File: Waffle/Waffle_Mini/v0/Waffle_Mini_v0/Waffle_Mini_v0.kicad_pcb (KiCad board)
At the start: 2 copper layers, 16 parts, among them J1 cJTAG, U1 F2800154QRHBRQ1, U2 AP7375-33SA-7

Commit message: Layout kinda done v0 waffle mini
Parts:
- removed C4, C7: 100n, Capacitor_SMD:C_0603_1608Metric
- removed C8: 10u, Capacitor_SMD:C_0805_2012Metric
- added J10: Conn_01x01_Socket, ICDB_Waffle:ICDB_Castellated_Pad, F.Cu at (139.7, 104.1)
- added J11: Conn_01x01_Socket, ICDB_Waffle:ICDB_Castellated_Pad, F.Cu at (142.2, 104.1)
- added J12: Conn_01x01_Socket, ICDB_Waffle:ICDB_Castellated_Pad, F.Cu at (144.8, 104.1)
- added J13: Conn_01x01_Socket, ICDB_Waffle:ICDB_Castellated_Pad, F.Cu at (147.3, 104.1)
- added J14: Conn_01x01_Socket, ICDB_Waffle:ICDB_Castellated_Pad, F.Cu at (149.9, 104.1)
- added J15: Conn_01x01_Socket, ICDB_Waffle:ICDB_Castellated_Pad, F.Cu at (152.4, 104.1)
- added J16: Conn_01x01_Socket, ICDB_Waffle:ICDB_Castellated_Pad, F.Cu at (154.9, 104.1)
- added J17: Conn_01x01_Socket, ICDB_Waffle:ICDB_Castellated_Pad, F.Cu at (157.5, 104.1)
- added J18: Conn_01x01_Socket, ICDB_Waffle:ICDB_Castellated_Pad, F.Cu at (160.0, 104.1)
- added J19: Conn_01x01_Socket, ICDB_Waffle:ICDB_Castellated_Pad, F.Cu at (162.6, 104.1)
- added J2: Conn_01x01_Socket, ICDB_Waffle:ICDB_Castellated_Pad, F.Cu at (157.5, 86.4)
- added J20: Conn_01x01_Socket, ICDB_Waffle:ICDB_Castellated_Pad, F.Cu at (165.1, 104.1)
- added J21: Conn_01x01_Socket, ICDB_Waffle:ICDB_Castellated_Pad, F.Cu at (165.1, 86.4)
- added J22: Conn_01x01_Socket, ICDB_Waffle:ICDB_Castellated_Pad, F.Cu at (162.6, 86.4)
- added J23: Conn_01x01_Socket, ICDB_Waffle:ICDB_Castellated_Pad, F.Cu at (160.0, 86.4)
- added J24: Conn_01x01_Socket, ICDB_Waffle:ICDB_Castellated_Pad, F.Cu at (134.6, 86.4)
- added J25: Conn_01x01_Socket, ICDB_Waffle:ICDB_Castellated_Pad, F.Cu at (134.6, 104.1)
- added J26: Conn_01x01_Socket, ICDB_Waffle:ICDB_Castellated_Pad, F.Cu at (137.2, 86.4)
- added J27: Conn_01x01_Socket, ICDB_Waffle:ICDB_Castellated_Pad, F.Cu at (137.2, 104.1)
- added J28: Conn_01x01_Socket, ICDB_Waffle:ICDB_Castellated_Pad, F.Cu at (167.6, 104.1)
- added J29: Conn_01x01_Socket, ICDB_Waffle:ICDB_Castellated_Pad, F.Cu at (167.6, 86.4)
- added J3: Conn_01x01_Socket, ICDB_Waffle:ICDB_Castellated_Pad, F.Cu at (154.9, 86.4)
- added J4: Conn_01x01_Socket, ICDB_Waffle:ICDB_Castellated_Pad, F.Cu at (152.4, 86.4)
- added J5: Conn_01x01_Socket, ICDB_Waffle:ICDB_Castellated_Pad, F.Cu at (149.9, 86.4)
- added J6: Conn_01x01_Socket, ICDB_Waffle:ICDB_Castellated_Pad, F.Cu at (147.3, 86.4)
- added J7: Conn_01x01_Socket, ICDB_Waffle:ICDB_Castellated_Pad, F.Cu at (144.8, 86.4)
- added J8: Conn_01x01_Socket, ICDB_Waffle:ICDB_Castellated_Pad, F.Cu at (142.2, 86.4)
- added J9: Conn_01x01_Socket, ICDB_Waffle:ICDB_Castellated_Pad, F.Cu at (139.7, 86.4)
- J1: value cJTAG -> Conn_ARM_SWD_TagConnect_TC2030-NL; footprint Connector_PinHeader_1.27mm:PinHeader_1x06_P1.27mm_Vertical_SMD_Pin1Left -> Connector:Tag-Connect_TC2030-IDC-NL_2x03_P1.27mm_Vertical
- moved C3 36.7 mm to (155.2, 98.9), turned to -90 degrees
- moved C1 35.3 mm to (151.7, 98.9), turned to 90 degrees
- moved R1 30.6 mm to (153.2, 98.9), turned to -90 degrees
- moved C5 29.9 mm to (157.0, 98.5), turned to -90 degrees
- moved R3 20.5 mm to (144.5, 96.1), turned to 90 degrees
- moved R2 20.4 mm to (144.5, 93.1), turned to -90 degrees
- moved C6 18.8 mm to (147.1, 92.9), turned to 180 degrees
- moved C9 18.5 mm to (138.3, 98.8), turned to -90 degrees
- moved U2 17.7 mm to (136.0, 95.6)
- moved J1 16.4 mm to (141.6, 95.2), turned to -90 degrees
- moved C2 13.6 mm to (135.8, 98.3)
- moved U1 7.67 mm to (152.2, 94.2), turned to -90 degrees
- moved C10 3.80 mm to (136.0, 92.1)
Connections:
- J1 pad 3: GND -> /XRSn
- J1 pad 6: /XRSn -> unconnected-(J1-SWO-Pad6)
- U1 pad 12: unconnected-(U1B-A4/C14-Pad12) -> Net-(J10-Pin_1)
- U1 pad 13: unconnected-(U1B-A10/C10_C8/A9_GPIO227_230-Pad13) -> Net-(J11-Pin_1)
- U1 pad 14: unconnected-(U1B-GPIO11-Pad14) -> Net-(J12-Pin_1)
- U1 pad 15: unconnected-(U1B-GPIO24-Pad15) -> Net-(J13-Pin_1)
- U1 pad 17: unconnected-(U1B-GPIO37_TDO-Pad17) -> Net-(J14-Pin_1)
- U1 pad 2: unconnected-(U1B-GPIO226_228_A6/C6-Pad2) -> Net-(J2-Pin_1)
- U1 pad 26: unconnected-(U1B-GPIO3-Pad26) -> Net-(J17-Pin_1)
- U1 pad 27: unconnected-(U1B-GPIO1-Pad27) -> Net-(J18-Pin_1)
- U1 pad 28: unconnected-(U1B-GPIO0-Pad28) -> Net-(J19-Pin_1)
- U1 pad 29: unconnected-(U1B-GPIO7-Pad29) -> Net-(J20-Pin_1)
- U1 pad 3: unconnected-(U1B-GPIO242_A3/C5-Pad3) -> Net-(J3-Pin_1)
- U1 pad 30: unconnected-(U1B-GPIO5-Pad30) -> Net-(J21-Pin_1)
- U1 pad 31: unconnected-(U1B-GPIO29-Pad31) -> Net-(J22-Pin_1)
- U1 pad 32: unconnected-(U1B-A16/C16_GPIO28-Pad32) -> Net-(J23-Pin_1)
- U1 pad 4: unconnected-(U1B-GPIO224_A2/C9-Pad4) -> Net-(J4-Pin_1)
- U1 pad 5: unconnected-(U1B-A15/C7_C4/A14-Pad5) -> Net-(J5-Pin_1)
- U1 pad 6: unconnected-(U1B-A11/C0_A5/C2-Pad6) -> Net-(J6-Pin_1)
- U1 pad 7: unconnected-(U1B-A0/C15/CMP1_DACL_A1-Pad7) -> Net-(J7-Pin_1)
- U1 pad 8: unconnected-(U1B-A12/C1_A7/C3-Pad8) -> Net-(J8-Pin_1)
- U1 pad 9: unconnected-(U1B-A8/C11-Pad9) -> Net-(J9-Pin_1)
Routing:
- net GND: track 0.00 -> 28.4 mm, vias 0 -> 16
- net /XRSn: track 0.00 -> 23.3 mm, vias 0 -> 2
- net Net-(J20-Pin_1): track 0.00 -> 15.3 mm
- net Net-(J10-Pin_1): track 0.00 -> 14.7 mm
- net Net-(J19-Pin_1): track 0.00 -> 13.2 mm
- net Net-(J21-Pin_1): track 0.00 -> 12.3 mm
- net Net-(J11-Pin_1): track 0.00 -> 11.9 mm
- net Net-(J9-Pin_1): track 0.00 -> 11.6 mm
- net /JTAG_TMS: track 0.00 -> 11.4 mm, vias 0 -> 2
- net Net-(J18-Pin_1): track 0.00 -> 10.8 mm
- net Net-(J17-Pin_1): track 0.00 -> 10.3 mm
- net Net-(J12-Pin_1): track 0.00 -> 9.59 mm
- net Net-(J22-Pin_1): track 0.00 -> 9.57 mm
- net Net-(J8-Pin_1): track 0.00 -> 9.47 mm
- net /JTAG_TCK: track 0.00 -> 8.85 mm, vias 0 -> 2
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- added copper zone on In1.Cu, net +3.3V
- added copper zone on In2.Cu, net GND
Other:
- board outline added: 35.6 x 17.8 mm
- copper layers 2 -> 4
- board text added: "Waffle Mini v0 12/23 Joseph A. De Vico"

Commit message: Curly added :)
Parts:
- added C11: 100n, Capacitor_SMD:C_0603_1608Metric, F.Cu at (138.8, 95.3)
- added R4: 4k7, Resistor_SMD:R_0603_1608Metric, F.Cu at (157.1, 91.5)
- moved C2 0.10 mm to (135.8, 98.2)
- moved U2 0.10 mm to (136.0, 95.5)
- moved C9 0.08 mm to (138.3, 98.7)
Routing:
- net GND: track 28.4 -> 30.3 mm
- net /XRSn: track 23.3 -> 24.3 mm
- net Net-(J23-Pin_1): track 7.46 -> 8.28 mm
- net Net-(J22-Pin_1): track 9.57 -> 10.3 mm
- net +3.3V: vias 8 -> 9

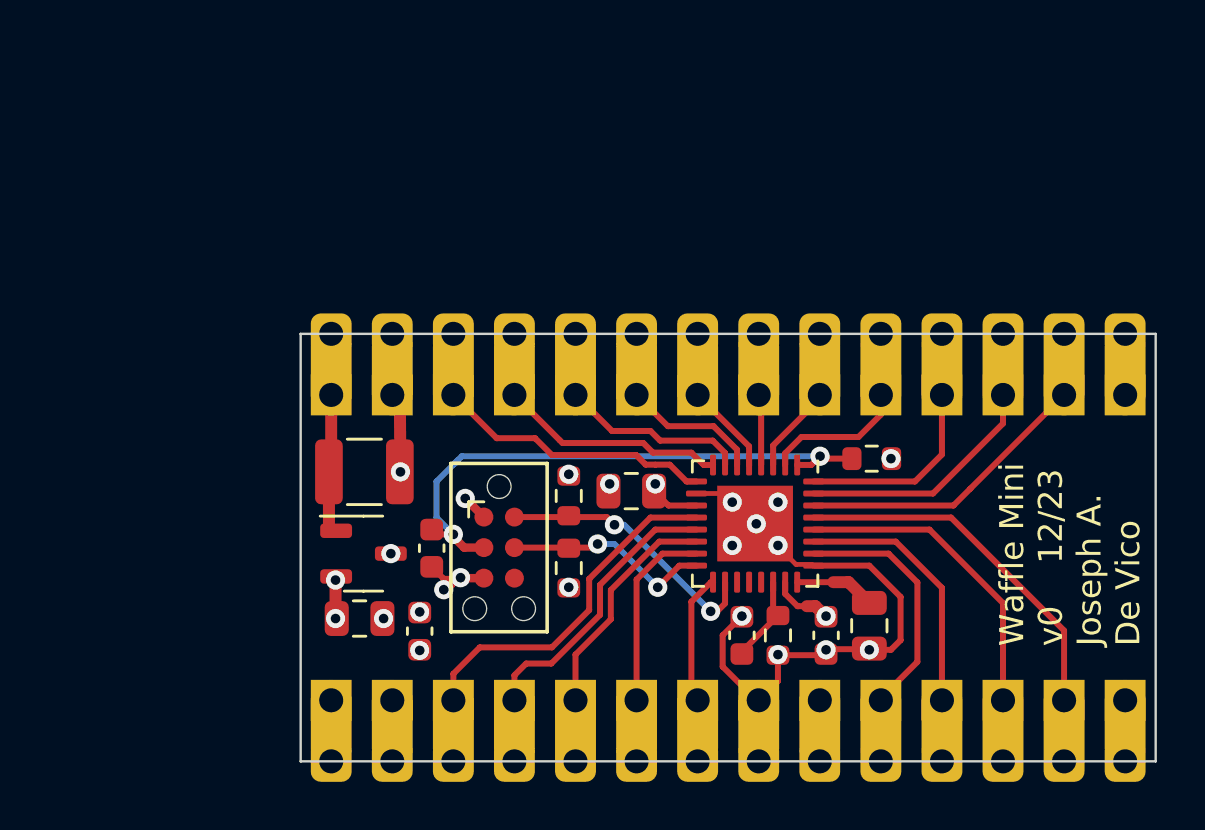
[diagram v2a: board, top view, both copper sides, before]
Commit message: Blinky works on Curly :) Added CAN transceiver to Waffle
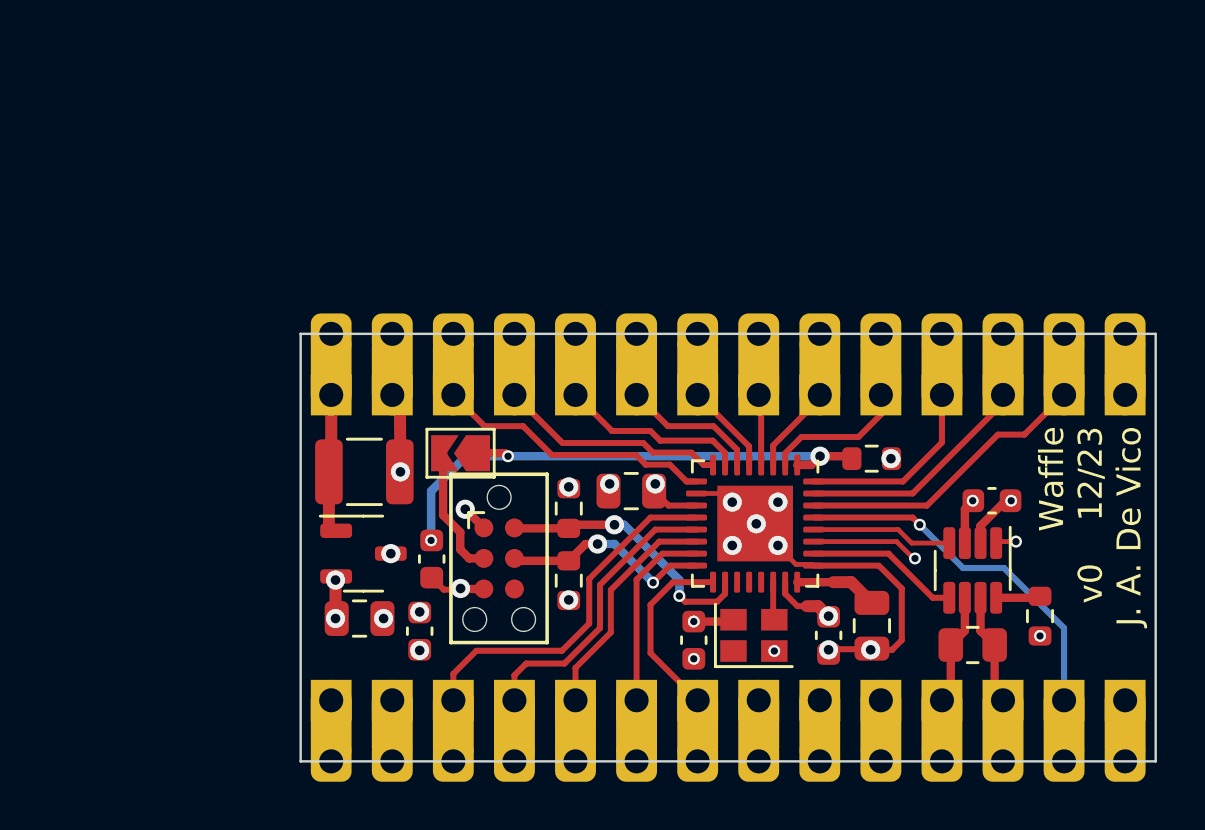
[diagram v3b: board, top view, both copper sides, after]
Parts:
- removed C1: 10n C0G?, Capacitor_SMD:C_0603_1608Metric
- removed R1: 100k 0.1%, Resistor_SMD:R_0603_1608Metric
- added C4: 100n, Capacitor_SMD:C_0603_1608Metric, F.Cu at (149.7, 99.1)
- added C7: 100n, Capacitor_SMD:C_0603_1608Metric, F.Cu at (162.1, 93.3)
- added JP1: SolderJumper_2_Open, Jumper:SolderJumper-2_P1.3mm_Open_TrianglePad1.0x1.5mm, F.Cu at (140.0, 91.3)
- added R5: 120R, Resistor_SMD:R_0805_2012Metric, F.Cu at (161.3, 99.3)
- added R6: 4k7, Resistor_SMD:R_0603_1608Metric, F.Cu at (164.1, 98.1)
- added U3: TCAN337, Package_TO_SOT_SMD:SOT-23-8, F.Cu at (161.3, 96.2)
- added X2: SG-210STF10.0000ML0, Oscillator:Oscillator_SMD_SeikoEpson_SG210-4Pin_2.5x2.0mm, F.Cu at (152.2, 98.9)
- C11: value 100n -> 10n
- moved R2 0.53 mm to (144.5, 93.6)
- moved R3 0.53 mm to (144.5, 96.6)
- moved J1 0.45 mm to (141.6, 95.7)
- moved C11 0.45 mm to (138.8, 95.7)
- moved C3 0.11 mm to (155.3, 98.9)
- moved C5 0.11 mm to (157.1, 98.5)
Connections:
- J1 pad 3: /XRSn -> Net-(J1-~{RESET})
- J17 pad 1: Net-(J17-Pin_1) -> GND
- J18 pad 1: Net-(J18-Pin_1) -> /CANL
- J19 pad 1: Net-(J19-Pin_1) -> /CANH
- U1 pad 26: Net-(J17-Pin_1) -> /CAN_FAULT
- U1 pad 27: Net-(J18-Pin_1) -> /CANTX
- U1 pad 28: Net-(J19-Pin_1) -> /CANRX
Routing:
- net Net-(J19-Pin_1): track 13.2 -> 0.00 mm
- net Net-(J18-Pin_1): track 10.8 -> 0.00 mm
- net /CANTX: track 0.00 -> 10.4 mm, vias 0 -> 2
- net Net-(J17-Pin_1): track 10.3 -> 0.00 mm
- net Net-(J1-~{RESET}): track 0.00 -> 8.01 mm
- net GND: track 30.3 -> 23.3 mm, vias 16 -> 17
- net /CAN_FAULT: track 0.00 -> 6.40 mm
- net /CANRX: track 0.00 -> 5.87 mm
- net /CANL: track 0.00 -> 4.66 mm
- net /CANH: track 0.00 -> 4.65 mm
- net +3.3V: track 7.76 -> 11.5 mm, vias 9 -> 11
- net Net-(J14-Pin_1): track 5.44 -> 7.77 mm
- net /XTAL_1: track 3.69 -> 1.58 mm
- net Net-(U3-S): track 0.00 -> 1.85 mm
- net /XRSn: track 24.3 -> 23.2 mm, vias 2 -> 3
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- added copper zone on In2.Cu, net +3.3V
- added copper zone on In1.Cu, net GND
- removed copper zone on In1.Cu, net +3.3V
- removed copper zone on In2.Cu, net GND
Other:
- board text added: "F2800154QRHBRQ1"
- board text added: "Waffle v0 12/23 J. A. De Vico"
- board text removed: "Waffle Mini v0 12/23 Joseph A. De Vico"
